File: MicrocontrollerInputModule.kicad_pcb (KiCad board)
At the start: 2 copper layers, 33.8 x 131 mm, 49 parts, among them J1 Conn_02x04_Odd_Even, J2 IPEX 20655-045E-01, U1 W25Q16JVUXIQ, U2 RP2040, U3 MCP23017_ML, Y1 12.000MHz

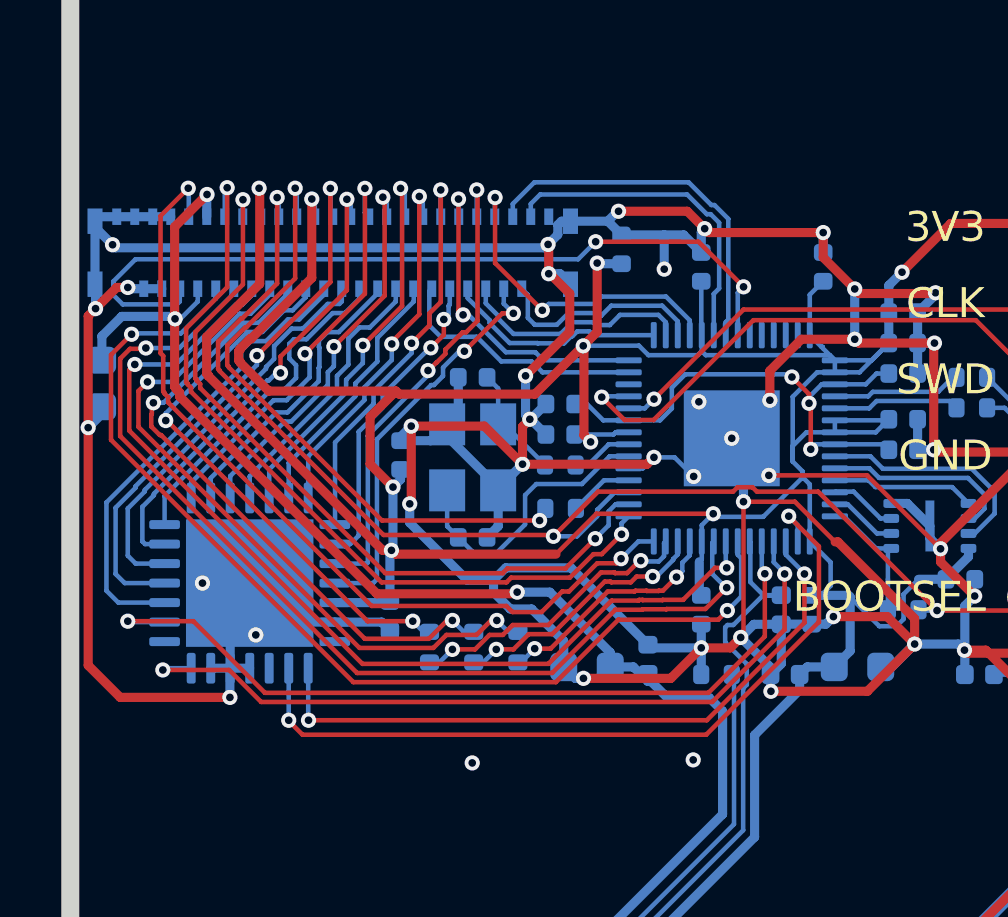
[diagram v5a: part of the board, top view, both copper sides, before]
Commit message: Switch to 23S17 from 23017
This increases the scan rate by ~5x (from 1.7MHz clock to 10MHz) and also
works around an erratum (?) in the 23017 which forces the A7 and B7 gpios
to be outputs.  This could lead to a short circuit if (for example)
a key on the same SENSE line is held down in both the A7 and some other
row -- A7 would be driven high (because it can't be three-stated) while
the other row is driven low, and a direct connection exists through
the two key switches.

The 23S17 part requires a few extra I/O pins, but we have some to spare.
Disconnected the INT pin from the I/O expander, because the way we would
do an interrupt is by driving all low on the 23S17 pins and then watching
for a low on the RP2040 GPIOs.  We shouldn't need to trigger an interrupt
on the DRV lines from the I/O expander.  But I pulled the INT line out to
a test point just in case.
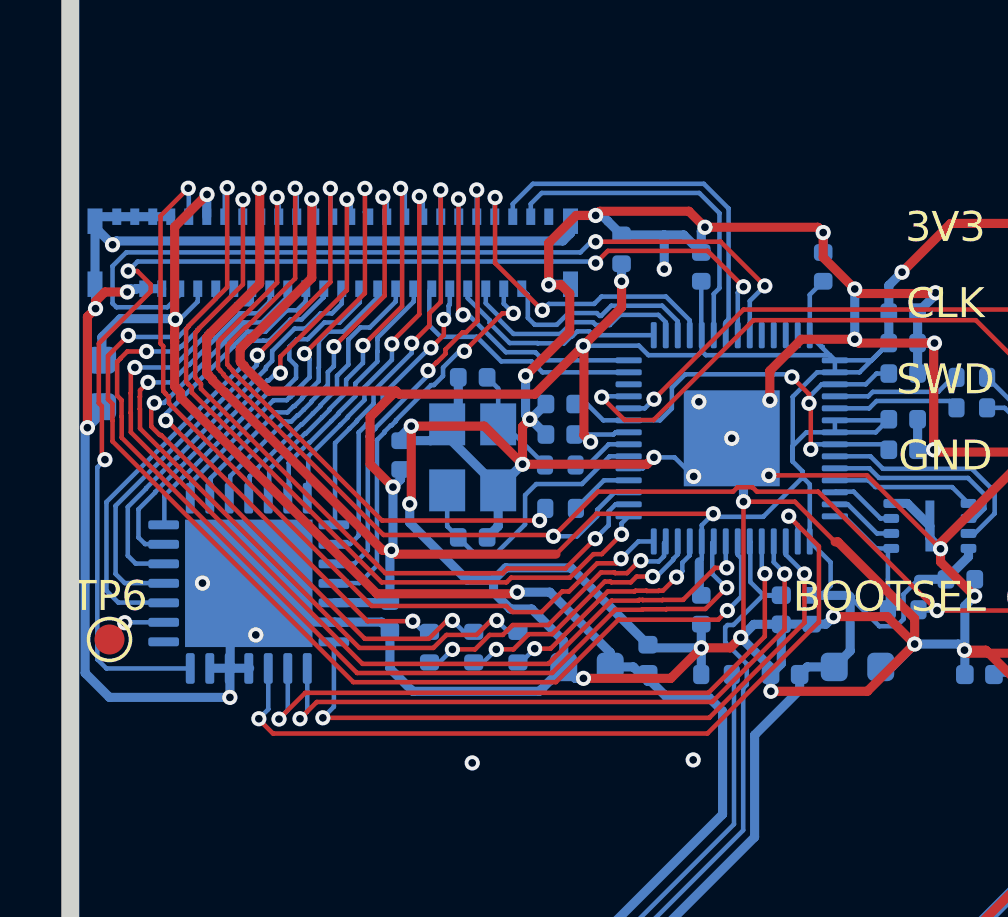
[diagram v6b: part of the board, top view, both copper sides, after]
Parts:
- added TP6: INT, TestPoint:TestPoint_Pad_D1.0mm, F.Cu at (51.3, 154.0)
- U3: value MCP23017_ML -> MCP23S17_ML
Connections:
- U2 pad 2: /IOEXP_SDA -> /IOEXP_MISO
- U2 pad 3: /IOEXP_SCK -> /~{IOEXP_CS}
- U2 pad 36: /~{KBD_BL_DET} -> /~{IOEXP_RESET}
- U2 pad 37: unconnected-(U2-GPIO25-Pad37) -> /~{KBD_BL_DET}
- U2 pad 4: /~{IOEXP_RESET} -> /IOEXP_SCK
- U2 pad 5: /IOEXP_INT -> /IOEXP_MOSI
- U3 pad 10: unconnected-(U3-NC-Pad10) -> /IOEXP_MISO
- U3 pad 16: /IOEXP_INT -> Net-(U3-INTA)
- U3 pad 7: unconnected-(U3-NC-Pad7) -> /~{IOEXP_CS}
- U3 pad 9: /IOEXP_SDA -> /IOEXP_MOSI
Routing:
- net /IOEXP_INT: track 27.4 -> 0.00 mm, vias 2 -> 0
- net /IOEXP_MISO: track 0.00 -> 27.1 mm, vias 0 -> 2
- net /IOEXP_SDA: track 26.1 -> 0.00 mm, vias 2 -> 0
- net /~{IOEXP_CS}: track 0.00 -> 23.0 mm, vias 0 -> 2
- net /IOEXP_MOSI: track 0.00 -> 22.4 mm, vias 0 -> 2
- net /~{IOEXP_RESET}: track 26.2 -> 40.6 mm, vias 2 -> 4
- net GND: track 250.7 -> 261.4 mm, vias 46 -> 45
- net Net-(U3-INTA): track 0.00 -> 2.07 mm, vias 0 -> 1
- net /~{KBD_BL_DET}: track 27.1 -> 28.5 mm
- net +3V3: track 147.4 -> 146.9 mm

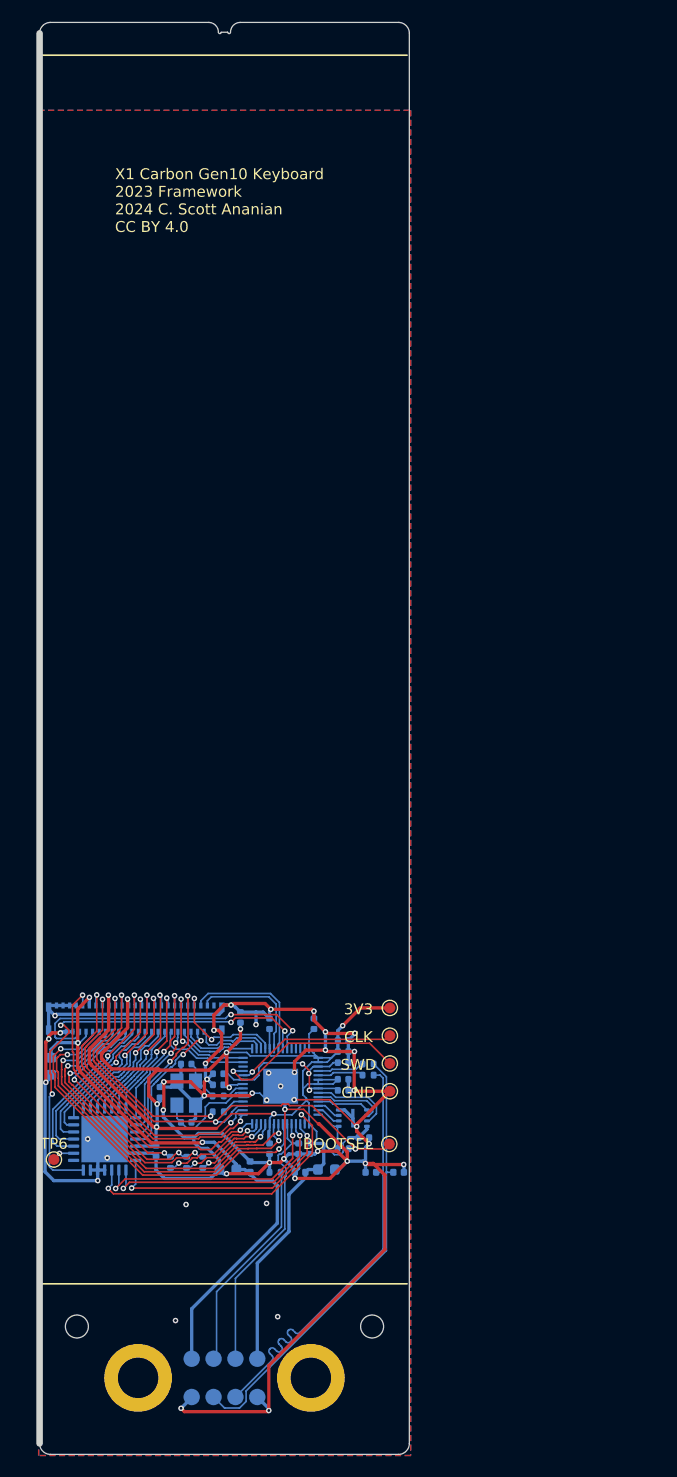
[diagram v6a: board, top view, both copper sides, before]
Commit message: Update with BOM information
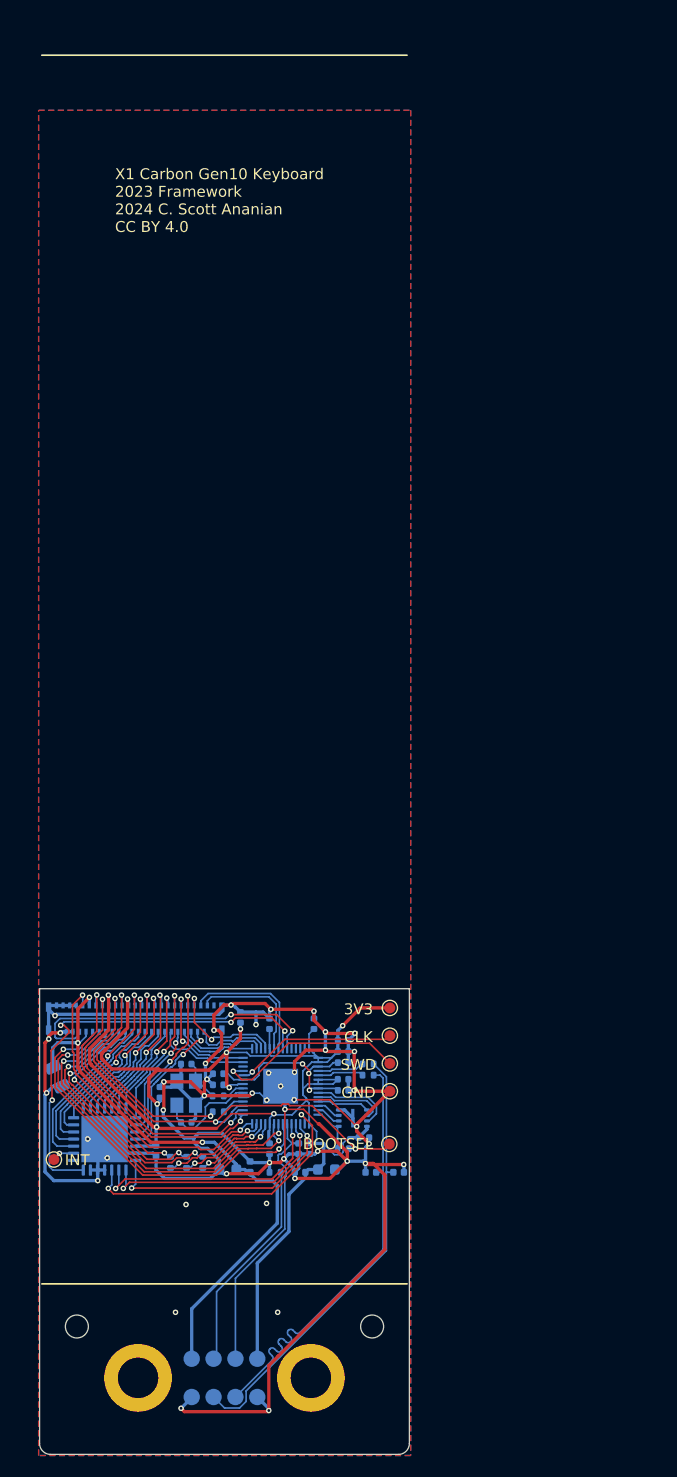
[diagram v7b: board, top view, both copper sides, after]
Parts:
- C19: footprint Capacitor_SMD:C_0603_1608Metric -> Capacitor_SMD:C_0805_2012Metric
- moved C19 1.12 mm to (51.6, 146.5), turned to 115 degrees
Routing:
- net GND: track 261.4 -> 262.2 mm
- net +5V: track 54.8 -> 55.5 mm
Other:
- board size 33.8 x 131 mm -> 33.8 x 42.6 mm
